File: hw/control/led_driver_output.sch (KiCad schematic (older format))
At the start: 9 parts

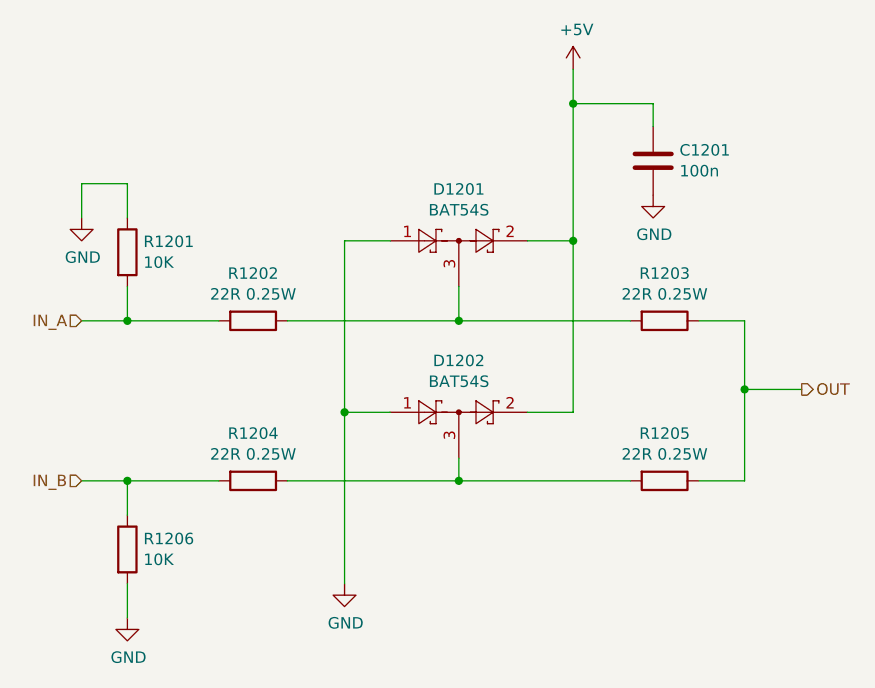
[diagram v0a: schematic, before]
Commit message: [hw] Update LED power supply
* Add 10 uF capacitors
* Add more space heat sinks
* Add thermal reliefs
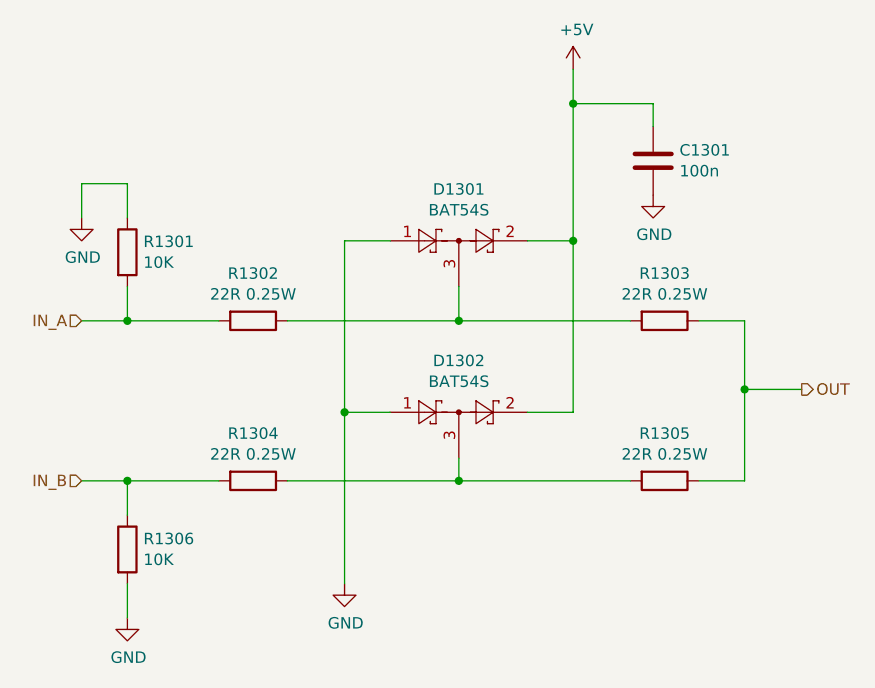
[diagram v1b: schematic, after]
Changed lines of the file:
@@
 AR Path="/614B1933/614A1815/614A3B39" Ref="R1202"  Part="1"
 AR Path="/614B1933/614AD8B5/614A3B39" Ref="R1302"  Part="1"
-F 0 "R1202" V 4743 3750 50  0000 C CNN
+F 0 "R1302" V 4743 3750 50  0000 C CNN
 F 1 "22R 0.25W" V 4834 3750 50  0000 C CNN
 F 2 "Resistor_SMD:R_1206_3216Metric_Pad1.30x1.75mm_HandSolder" V 4880 3750 50  0001 C CNN
@@
 AR Path="/614B1933/614A1815/614A3B3F" Ref="R1203"  Part="1"
 AR Path="/614B1933/614AD8B5/614A3B3F" Ref="R1303"  Part="1"
-F 0 "R1203" V 6543 3750 50  0000 C CNN
+F 0 "R1303" V 6543 3750 50  0000 C CNN
 F 1 "22R 0.25W" V 6634 3750 50  0000 C CNN
 F 2 "Resistor_SMD:R_1206_3216Metric_Pad1.30x1.75mm_HandSolder" V 6680 3750 50  0001 C CNN
@@
 AR Path="/614B1933/614A1815/614A3B45" Ref="R1204"  Part="1"
 AR Path="/614B1933/614AD8B5/614A3B45" Ref="R1304"  Part="1"
-F 0 "R1204" V 4743 4450 50  0000 C CNN
+F 0 "R1304" V 4743 4450 50  0000 C CNN
 F 1 "22R 0.25W" V 4834 4450 50  0000 C CNN
 F 2 "Resistor_SMD:R_1206_3216Metric_Pad1.30x1.75mm_HandSolder" V 4880 4450 50  0001 C CNN
@@
 AR Path="/614B1933/614A1815/614A3B4B" Ref="R1205"  Part="1"
 AR Path="/614B1933/614AD8B5/614A3B4B" Ref="R1305"  Part="1"
-F 0 "R1205" V 6543 4450 50  0000 C CNN
+F 0 "R1305" V 6543 4450 50  0000 C CNN
 F 1 "22R 0.25W" V 6634 4450 50  0000 C CNN
 F 2 "Resistor_SMD:R_1206_3216Metric_Pad1.30x1.75mm_HandSolder" V 6680 4450 50  0001 C CNN
@@
 AR Path="/614B1933/614A1815/614A3B70" Ref="#PWR01201"  Part="1"
 AR Path="/614B1933/614AD8B5/614A3B70" Ref="#PWR01301"  Part="1"
-F 0 "#PWR01201" H 6350 2500 50  0001 C CNN
+F 0 "#PWR01301" H 6350 2500 50  0001 C CNN
 F 1 "+5V" H 6365 2823 50  0000 C CNN
 F 2 "" H 6350 2650 50  0001 C CNN
@@
 AR Path="/614B1933/614A1815/614A4F14" Ref="#PWR01203"  Part="1"
 AR Path="/614B1933/614AD8B5/614A4F14" Ref="#PWR01303"  Part="1"
-F 0 "#PWR01203" H 5350 4650 50  0001 C CNN
+F 0 "#PWR01303" H 5350 4650 50  0001 C CNN
 F 1 "GND" H 5355 4727 50  0000 C CNN
 F 2 "" H 5350 4900 50  0001 C CNN
@@
 AR Path="/614B1933/614A1815/616363D2" Ref="R1201"  Part="1"
 AR Path="/614B1933/614AD8B5/616363D2" Ref="R1301"  Part="1"
-F 0 "R1201" H 4470 3496 50  0000 L CNN
+F 0 "R1301" H 4470 3496 50  0000 L CNN
 F 1 "10K" H 4470 3405 50  0000 L CNN
 F 2 "Resistor_SMD:R_0805_2012Metric_Pad1.20x1.40mm_HandSolder" V 4330 3450 50  0001 C CNN
@@
 AR Path="/614B1933/614A1815/61637113" Ref="R1206"  Part="1"
 AR Path="/614B1933/614AD8B5/61637113" Ref="R1306"  Part="1"
-F 0 "R1206" H 4470 4796 50  0000 L CNN
+F 0 "R1306" H 4470 4796 50  0000 L CNN
 F 1 "10K" H 4470 4705 50  0000 L CNN
 F 2 "Resistor_SMD:R_0805_2012Metric_Pad1.20x1.40mm_HandSolder" V 4330 4750 50  0001 C CNN
@@
 AR Path="/614B1933/614A1815/61637D81" Ref="#PWR01202"  Part="1"
 AR Path="/614B1933/614AD8B5/61637D81" Ref="#PWR01302"  Part="1"
-F 0 "#PWR01202" H 4200 3050 50  0001 C CNN
+F 0 "#PWR01302" H 4200 3050 50  0001 C CNN
 F 1 "GND" H 4205 3127 50  0000 C CNN
 F 2 "" H 4200 3300 50  0001 C CNN
@@
 AR Path="/614B1933/614A1815/6163895E" Ref="#PWR01204"  Part="1"
 AR Path="/614B1933/614AD8B5/6163895E" Ref="#PWR01304"  Part="1"
-F 0 "#PWR01204" H 4400 4800 50  0001 C CNN
+F 0 "#PWR01304" H 4400 4800 50  0001 C CNN
 F 1 "GND" H 4405 4877 50  0000 C CNN
 F 2 "" H 4400 5050 50  0001 C CNN
@@
 AR Path="/614B1933/614A1815/616BDFA1" Ref="C1201"  Part="1"
 AR Path="/614B1933/614AD8B5/616BDFA1" Ref="C1301"  Part="1"
-F 0 "C1201" H 6815 3096 50  0000 L CNN
+F 0 "C1301" H 6815 3096 50  0000 L CNN
 F 1 "100n" H 6815 3005 50  0000 L CNN
 F 2 "Capacitor_SMD:C_0805_2012Metric_Pad1.18x1.45mm_HandSolder" H 6738 2900 50  0001 C CNN
@@
 AR Path="/614B1933/614A1815/616BEE8A" Ref="#PWR01205"  Part="1"
 AR Path="/614B1933/614AD8B5/616BEE8A" Ref="#PWR01305"  Part="1"
-F 0 "#PWR01205" H 6700 2950 50  0001 C CNN
+F 0 "#PWR01305" H 6700 2950 50  0001 C CNN
 F 1 "GND" H 6705 3027 50  0000 C CNN
 F 2 "" H 6700 3200 50  0001 C CNN
@@
 AR Path="/614B1933/614A1815/616B883B" Ref="D1201"  Part="1"
 AR Path="/614B1933/614AD8B5/616B883B" Ref="D1301"  Part="1"
-F 0 "D1201" H 5850 3625 50  0000 C CNN
+F 0 "D1301" H 5850 3625 50  0000 C CNN
 F 1 "BAT54S" H 5850 3534 50  0000 C CNN
 F 2 "Package_TO_SOT_SMD:SOT-23" H 5925 3525 50  0001 L CNN
@@
 AR Path="/614B1933/614A1815/616B92EE" Ref="D1202"  Part="1"
 AR Path="/614B1933/614AD8B5/616B92EE" Ref="D1302"  Part="1"
-F 0 "D1202" H 5850 4375 50  0000 C CNN
+F 0 "D1302" H 5850 4375 50  0000 C CNN
 F 1 "BAT54S" H 5850 4284 50  0000 C CNN
 F 2 "Package_TO_SOT_SMD:SOT-23" H 5925 4275 50  0001 L CNN

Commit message: [hw] Add layout of multiple subsystems
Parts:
- D1201, D1202: footprint Package_TO_SOT_SMD:SOT-23 -> Package_TO_SOT_SMD:SOT-23_Handsoldering
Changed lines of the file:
@@
 $Descr A4 11693 8268
 encoding utf-8
-Sheet 12 13
+Sheet 13 13
 Title "WS2812 Controller"
 Date "2021-10-10"
@@
 F 0 "D1301" H 5850 3625 50  0000 C CNN
 F 1 "BAT54S" H 5850 3534 50  0000 C CNN
-F 2 "Package_TO_SOT_SMD:SOT-23" H 5925 3525 50  0001 L CNN
+F 2 "Package_TO_SOT_SMD:SOT-23_Handsoldering" H 5925 3525 50  0001 L CNN
 F 3 "https://www.diodes.com/assets/Datasheets/ds11005.pdf" H 5730 3400 50  0001 C CNN
 	1    5850 3400
@@
 F 0 "D1302" H 5850 4375 50  0000 C CNN
 F 1 "BAT54S" H 5850 4284 50  0000 C CNN
-F 2 "Package_TO_SOT_SMD:SOT-23" H 5925 4275 50  0001 L CNN
+F 2 "Package_TO_SOT_SMD:SOT-23_Handsoldering" H 5925 4275 50  0001 L CNN
 F 3 "https://www.diodes.com/assets/Datasheets/ds11005.pdf" H 5730 4150 50  0001 C CNN
 	1    5850 4150

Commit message: [hw] Re-annotate all components
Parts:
- renumbered C1201 to C1401, D1201 to D1401, D1202 to D1402, R1201 to R1401, R1202 to R1402, R1203 to R1403, R1204 to R1404, R1205 to R1405, R1206 to R1406
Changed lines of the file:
@@
 P 4950 3750
 AR Path="/614B1933/614A3B39" Ref="R?"  Part="1"
-AR Path="/614B1933/614A1815/614A3B39" Ref="R1202"  Part="1"
-AR Path="/614B1933/614AD8B5/614A3B39" Ref="R1302"  Part="1"
-F 0 "R1302" V 4743 3750 50  0000 C CNN
+AR Path="/614B1933/614A1815/614A3B39" Ref="R1402"  Part="1"
+AR Path="/614B1933/614AD8B5/614A3B39" Ref="R1502"  Part="1"
+F 0 "R1502" V 4743 3750 50  0000 C CNN
 F 1 "22R 0.25W" V 4834 3750 50  0000 C CNN
 F 2 "Resistor_SMD:R_1206_3216Metric_Pad1.30x1.75mm_HandSolder" V 4880 3750 50  0001 C CNN
@@
 P 6750 3750
 AR Path="/614B1933/614A3B3F" Ref="R?"  Part="1"
-AR Path="/614B1933/614A1815/614A3B3F" Ref="R1203"  Part="1"
-AR Path="/614B1933/614AD8B5/614A3B3F" Ref="R1303"  Part="1"
-F 0 "R1303" V 6543 3750 50  0000 C CNN
+AR Path="/614B1933/614A1815/614A3B3F" Ref="R1403"  Part="1"
+AR Path="/614B1933/614AD8B5/614A3B3F" Ref="R1503"  Part="1"
+F 0 "R1503" V 6543 3750 50  0000 C CNN
 F 1 "22R 0.25W" V 6634 3750 50  0000 C CNN
 F 2 "Resistor_SMD:R_1206_3216Metric_Pad1.30x1.75mm_HandSolder" V 6680 3750 50  0001 C CNN
@@
 P 4950 4450
 AR Path="/614B1933/614A3B45" Ref="R?"  Part="1"
-AR Path="/614B1933/614A1815/614A3B45" Ref="R1204"  Part="1"
-AR Path="/614B1933/614AD8B5/614A3B45" Ref="R1304"  Part="1"
-F 0 "R1304" V 4743 4450 50  0000 C CNN
+AR Path="/614B1933/614A1815/614A3B45" Ref="R1404"  Part="1"
+AR Path="/614B1933/614AD8B5/614A3B45" Ref="R1504"  Part="1"
+F 0 "R1504" V 4743 4450 50  0000 C CNN
 F 1 "22R 0.25W" V 4834 4450 50  0000 C CNN
 F 2 "Resistor_SMD:R_1206_3216Metric_Pad1.30x1.75mm_HandSolder" V 4880 4450 50  0001 C CNN
@@
 P 6750 4450
 AR Path="/614B1933/614A3B4B" Ref="R?"  Part="1"
-AR Path="/614B1933/614A1815/614A3B4B" Ref="R1205"  Part="1"
-AR Path="/614B1933/614AD8B5/614A3B4B" Ref="R1305"  Part="1"
-F 0 "R1305" V 6543 4450 50  0000 C CNN
+AR Path="/614B1933/614A1815/614A3B4B" Ref="R1405"  Part="1"
+AR Path="/614B1933/614AD8B5/614A3B4B" Ref="R1505"  Part="1"
+F 0 "R1505" V 6543 4450 50  0000 C CNN
 F 1 "22R 0.25W" V 6634 4450 50  0000 C CNN
 F 2 "Resistor_SMD:R_1206_3216Metric_Pad1.30x1.75mm_HandSolder" V 6680 4450 50  0001 C CNN
@@
 P 6350 2650
 AR Path="/614B1933/614A3B70" Ref="#PWR?"  Part="1"
-AR Path="/614B1933/614A1815/614A3B70" Ref="#PWR01201"  Part="1"
-AR Path="/614B1933/614AD8B5/614A3B70" Ref="#PWR01301"  Part="1"
-F 0 "#PWR01301" H 6350 2500 50  0001 C CNN
+AR Path="/614B1933/614A1815/614A3B70" Ref="#PWR01401"  Part="1"
+AR Path="/614B1933/614AD8B5/614A3B70" Ref="#PWR01501"  Part="1"
+F 0 "#PWR01501" H 6350 2500 50  0001 C CNN
 F 1 "+5V" H 6365 2823 50  0000 C CNN
 F 2 "" H 6350 2650 50  0001 C CNN
@@
 Connection ~ 5350 4150
 $Comp
-L power:GND #PWR01203
+L power:GND #PWR01404
 U 1 1 614A4F14
 P 5350 4900
-AR Path="/614B1933/614A1815/614A4F14" Ref="#PWR01203"  Part="1"
-AR Path="/614B1933/614AD8B5/614A4F14" Ref="#PWR01303"  Part="1"
-F 0 "#PWR01303" H 5350 4650 50  0001 C CNN
+AR Path="/614B1933/614A1815/614A4F14" Ref="#PWR01404"  Part="1"
+AR Path="/614B1933/614AD8B5/614A4F14" Ref="#PWR01504"  Part="1"
+F 0 "#PWR01504" H 5350 4650 50  0001 C CNN
 F 1 "GND" H 5355 4727 50  0000 C CNN
 F 2 "" H 5350 4900 50  0001 C CNN
@@
 	4200 3750 4400 3750
 $Comp
-L Device:R R1201
+L Device:R R1401
 U 1 1 616363D2
 P 4400 3450
-AR Path="/614B1933/614A1815/616363D2" Ref="R1201"  Part="1"
-AR Path="/614B1933/614AD8B5/616363D2" Ref="R1301"  Part="1"
-F 0 "R1301" H 4470 3496 50  0000 L CNN
+AR Path="/614B1933/614A1815/616363D2" Ref="R1401"  Part="1"
+AR Path="/614B1933/614AD8B5/616363D2" Ref="R1501"  Part="1"
+F 0 "R1501" H 4470 3496 50  0000 L CNN
 F 1 "10K" H 4470 3405 50  0000 L CNN
 F 2 "Resistor_SMD:R_0805_2012Metric_Pad1.20x1.40mm_HandSolder" V 4330 3450 50  0001 C CNN
@@
 $EndComp
 $Comp
-L Device:R R1206
+L Device:R R1406
 U 1 1 61637113
 P 4400 4750
-AR Path="/614B1933/614A1815/61637113" Ref="R1206"  Part="1"
-AR Path="/614B1933/614AD8B5/61637113" Ref="R1306"  Part="1"
-F 0 "R1306" H 4470 4796 50  0000 L CNN
+AR Path="/614B1933/614A1815/61637113" Ref="R1406"  Part="1"
+AR Path="/614B1933/614AD8B5/61637113" Ref="R1506"  Part="1"
+F 0 "R1506" H 4470 4796 50  0000 L CNN
 F 1 "10K" H 4470 4705 50  0000 L CNN
 F 2 "Resistor_SMD:R_0805_2012Metric_Pad1.20x1.40mm_HandSolder" V 4330 4750 50  0001 C CNN
@@
 $EndComp
 $Comp
-L power:GND #PWR01202
+L power:GND #PWR01403
 U 1 1 61637D81
 P 4200 3300
-AR Path="/614B1933/614A1815/61637D81" Ref="#PWR01202"  Part="1"
-AR Path="/614B1933/614AD8B5/61637D81" Ref="#PWR01302"  Part="1"
-F 0 "#PWR01302" H 4200 3050 50  0001 C CNN
+AR Path="/614B1933/614A1815/61637D81" Ref="#PWR01403"  Part="1"
+AR Path="/614B1933/614AD8B5/61637D81" Ref="#PWR01503"  Part="1"
+F 0 "#PWR01503" H 4200 3050 50  0001 C CNN
 F 1 "GND" H 4205 3127 50  0000 C CNN
 F 2 "" H 4200 3300 50  0001 C CNN
@@
 $EndComp
 $Comp
-L power:GND #PWR01204
+L power:GND #PWR01405
 U 1 1 6163895E
 P 4400 5050
-AR Path="/614B1933/614A1815/6163895E" Ref="#PWR01204"  Part="1"
-AR Path="/614B1933/614AD8B5/6163895E" Ref="#PWR01304"  Part="1"
-F 0 "#PWR01304" H 4400 4800 50  0001 C CNN
+AR Path="/614B1933/614A1815/6163895E" Ref="#PWR01405"  Part="1"
+AR Path="/614B1933/614AD8B5/6163895E" Ref="#PWR01505"  Part="1"
+F 0 "#PWR01505" H 4400 4800 50  0001 C CNN
 F 1 "GND" H 4405 4877 50  0000 C CNN
 F 2 "" H 4400 5050 50  0001 C CNN
@@
 	4200 3150 4200 3300
 $Comp
-L Device:C C1201
+L Device:C C1401
 U 1 1 616BDFA1
 P 6700 3050
-AR Path="/614B1933/614A1815/616BDFA1" Ref="C1201"  Part="1"
-AR Path="/614B1933/614AD8B5/616BDFA1" Ref="C1301"  Part="1"
-F 0 "C1301" H 6815 3096 50  0000 L CNN
+AR Path="/614B1933/614A1815/616BDFA1" Ref="C1401"  Part="1"
+AR Path="/614B1933/614AD8B5/616BDFA1" Ref="C1501"  Part="1"
+F 0 "C1501" H 6815 3096 50  0000 L CNN
 F 1 "100n" H 6815 3005 50  0000 L CNN
 F 2 "Capacitor_SMD:C_0805_2012Metric_Pad1.18x1.45mm_HandSolder" H 6738 2900 50  0001 C CNN
@@
 $EndComp
 $Comp
-L power:GND #PWR01205
+L power:GND #PWR01402
 U 1 1 616BEE8A
 P 6700 3200
-AR Path="/614B1933/614A1815/616BEE8A" Ref="#PWR01205"  Part="1"
-AR Path="/614B1933/614AD8B5/616BEE8A" Ref="#PWR01305"  Part="1"
-F 0 "#PWR01305" H 6700 2950 50  0001 C CNN
+AR Path="/614B1933/614A1815/616BEE8A" Ref="#PWR01402"  Part="1"
+AR Path="/614B1933/614AD8B5/616BEE8A" Ref="#PWR01502"  Part="1"
+F 0 "#PWR01502" H 6700 2950 50  0001 C CNN
 F 1 "GND" H 6705 3027 50  0000 C CNN
 F 2 "" H 6700 3200 50  0001 C CNN
@@
 $EndComp
 $Comp
-L Diode:BAT54S D1201
+L Diode:BAT54S D1401
 U 1 1 616B883B
 P 5850 3400
-AR Path="/614B1933/614A1815/616B883B" Ref="D1201"  Part="1"
-AR Path="/614B1933/614AD8B5/616B883B" Ref="D1301"  Part="1"
-F 0 "D1301" H 5850 3625 50  0000 C CNN
+AR Path="/614B1933/614A1815/616B883B" Ref="D1401"  Part="1"
+AR Path="/614B1933/614AD8B5/616B883B" Ref="D1501"  Part="1"
+F 0 "D1501" H 5850 3625 50  0000 C CNN
 F 1 "BAT54S" H 5850 3534 50  0000 C CNN
 F 2 "Package_TO_SOT_SMD:SOT-23_Handsoldering" H 5925 3525 50  0001 L CNN
@@
 $EndComp
 $Comp
-L Diode:BAT54S D1202
+L Diode:BAT54S D1402
 U 1 1 616B92EE
 P 5850 4150
-AR Path="/614B1933/614A1815/616B92EE" Ref="D1202"  Part="1"
-AR Path="/614B1933/614AD8B5/616B92EE" Ref="D1302"  Part="1"
-F 0 "D1302" H 5850 4375 50  0000 C CNN
+AR Path="/614B1933/614A1815/616B92EE" Ref="D1402"  Part="1"
+AR Path="/614B1933/614AD8B5/616B92EE" Ref="D1502"  Part="1"
+F 0 "D1502" H 5850 4375 50  0000 C CNN
 F 1 "BAT54S" H 5850 4284 50  0000 C CNN
 F 2 "Package_TO_SOT_SMD:SOT-23_Handsoldering" H 5925 4275 50  0001 L CNN
